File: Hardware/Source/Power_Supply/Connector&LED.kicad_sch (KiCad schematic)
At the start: 13 parts, among them J2 Conn_01x09_Socket

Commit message: update
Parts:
- J2: footprint (none) -> Connector_PinHeader_1.00mm:PinHeader_1x09_P1.00mm_Vertical
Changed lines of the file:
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@@
 			)
 		)
-		(property "Footprint" ""
+		(property "Footprint" "Connector_PinHeader_1.00mm:PinHeader_1x09_P1.00mm_Vertical"
 			(at 101.6 69.85 0)
 			(effects

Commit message: update
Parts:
- removed J2: Conn_01x09_Socket, Connector_PinHeader_1.00mm:PinHeader_1x09_P1.00mm_Vertical, symbol Connector:Conn_01x09_Socket
- added J2, J3: Conn_01x06_Socket, Connector_Phoenix_MC:PhoenixContact_MC_1,5_6-G-3.81_1x06_P3.81mm_Horizontal, symbol Connector:Conn_01x06_Socket
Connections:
- net +12V: now also J2.1 (Pin_1)
- net +5V: now also J2.4 (Pin_4), J3.1 (Pin_1)
- net +9V: now also J2.2 (Pin_2), J3.4 (Pin_4)
- net -9_1V: now also J3.5 (Pin_5)
- net -9_2V: now also J2.3 (Pin_3)
- net GND2: now also J2.6 (Pin_6), J3.6 (Pin_6)
- new net +3.3_1V: J3.2 (Pin_2)
- new net +3.3_2V: J3.3 (Pin_3)
- new net +3.3_3V: J2.5 (Pin_5)

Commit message: update flyback co 7V
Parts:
- added J4: Conn_01x02_Socket, Connector_Phoenix_MC:PhoenixContact_MC_1,5_2-G-3.5_1x02_P3.50mm_Horizontal, symbol Connector:Conn_01x02_Socket
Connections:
- net +5V: no longer J2.4 (Pin_4), J3.1 (Pin_1)
- new net +5_1V: J4.1 (Pin_1)
- new net +5_2V: J2.4 (Pin_4), J3.1 (Pin_1)
- new net GND3: J4.2 (Pin_2)
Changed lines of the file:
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@@
+	(wire
+		(pts
+			(xy 86.36 76.2) (xy 86.36 74.93)
+		)
+		(stroke
+			(width 0)
+			(type default)
+		)
+	)
 	(wire
 		(pts
@@
 	(wire
 		(pts
+			(xy 86.36 78.74) (xy 86.36 81.28)
+		)
+		(stroke
+			(width 0)
+			(type default)
+		)
+	)
+	(wire
+		(pts
 			(xy 59.69 102.87) (xy 90.17 102.87)
 		)
@@
 	(wire
 		(pts
+			(xy 90.17 76.2) (xy 86.36 76.2)
+		)
+		(stroke
+			(width 0)
+			(type default)
+		)
+	)
+	(wire
+		(pts
 			(xy 190.5 55.88) (xy 190.5 58.42)
 		)
@@
 		(pts
 			(xy 77.47 97.79) (xy 90.17 97.79)
+		)
+		(stroke
+			(width 0)
+			(type default)
+		)
+	)
+	(wire
+		(pts
+			(xy 90.17 78.74) (xy 86.36 78.74)
 		)
 		(stroke
@@
 	)
 	(symbol
+		(lib_id "Connector:Conn_01x02_Socket")
+		(at 95.25 76.2 0)
+		(unit 1)
+		(exclude_from_sim no)
+		(in_bom yes)
+		(on_board yes)
+		(dnp no)
+		(fields_autoplaced yes)
+		(property "Reference" "J4"
+			(at 96.52 76.1999 0)
+			(effects
+				(font
+					(size 1.27 1.27)
+				)
+				(justify left)
+			)
+		)
+		(property "Value" "Conn_01x02_Socket"
+			(at 96.52 78.7399 0)
+			(effects
+				(font
+					(size 1.27 1.27)
+				)
+				(justify left)
+			)
+		)
+		(property "Footprint" "Connector_Phoenix_MC:PhoenixContact_MC_1,5_2-G-3.5_1x02_P3.50mm_Horizontal"
+			(at 95.25 76.2 0)
+			(effects
+				(font
+					(size 1.27 1.27)
+				)
+				(hide yes)
+			)
+		)
+		(property "Datasheet" "~"
+			(at 95.25 76.2 0)
+			(effects
+				(font
+					(size 1.27 1.27)
+				)
+				(hide yes)
+			)
+		)
+		(property "Description" "Generic connector, single row, 01x02, script generated"
+			(at 95.25 76.2 0)
+			(effects
+				(font
+					(size 1.27 1.27)
+				)
+				(hide yes)
+			)
+		)
+		(pin "2"
+		)
+		(pin "1"
+		)
+		(instances
+			(project ""
+				(path "/5c8a7907-026b-4416-b231-5ef9f93b99e1/68308591-2b49-42fc-9085-b4eeb0133b73"
+					(reference "J4")
+					(unit 1)
+				)
+			)
+		)
+	)
+	(symbol
 		(lib_id "power:GND2")
 		(at 190.5 109.22 0)
@@
 			)
 		)
-		(property "Value" "+5V"
+		(property "Value" "+5_2V"
 			(at 63.5 129.286 0)
 			(effects
@@
 				(path "/5c8a7907-026b-4416-b231-5ef9f93b99e1/68308591-2b49-42fc-9085-b4eeb0133b73"
 					(reference "R26")
+					(unit 1)
+				)
+			)
+		)
+	)
+	(symbol
+		(lib_id "power:+3.3V")
+		(at 86.36 74.93 0)
+		(unit 1)
+		(exclude_from_sim no)
+		(in_bom yes)
+		(on_board yes)
+		(dnp no)
+		(property "Reference" "#PWR065"
+			(at 86.36 78.74 0)
+			(effects
+				(font
+					(size 1.27 1.27)
+				)
+				(hide yes)
+			)
+		)
+		(property "Value" "+5_1V"
+			(at 86.36 71.374 0)
+			(effects
+				(font
+					(size 1.27 1.27)
+				)
+			)
+		)
+		(property "Footprint" ""
+			(at 86.36 74.93 0)
+			(effects
+				(font
+					(size 1.27 1.27)
+				)
+				(hide yes)
+			)
+		)
+		(property "Datasheet" ""
+			(at 86.36 74.93 0)
+			(effects
+				(font
+					(size 1.27 1.27)
+				)
+				(hide yes)
+			)
+		)
+		(property "Description" "Power symbol creates a global label with name \"+3.3V\""
+			(at 86.36 74.93 0)
+			(effects
+				(font
+					(size 1.27 1.27)
+				)
+				(hide yes)
+			)
+		)
+		(pin "1"
+		)
+		(instances
+			(project "Power_Supply"
+				(path "/5c8a7907-026b-4416-b231-5ef9f93b99e1/68308591-2b49-42fc-9085-b4eeb0133b73"
+					(reference "#PWR065")
 					(unit 1)
 				)
@@
 	)
 	(symbol
+		(lib_id "power:GND2")
+		(at 86.36 81.28 0)
+		(unit 1)
+		(exclude_from_sim no)
+		(in_bom yes)
+		(on_board yes)
+		(dnp no)
+		(fields_autoplaced yes)
+		(property "Reference" "#PWR066"
+			(at 86.36 87.63 0)
+			(effects
+				(font
+					(size 1.27 1.27)
+				)
+				(hide yes)
+			)
+		)
+		(property "Value" "GND3"
+			(at 86.36 86.36 0)
+			(effects
+				(font
+					(size 1.27 1.27)
+				)
+			)
+		)
+		(property "Footprint" ""
+			(at 86.36 81.28 0)
+			(effects
+				(font
+					(size 1.27 1.27)
+				)
+				(hide yes)
+			)
+		)
+		(property "Datasheet" ""
+			(at 86.36 81.28 0)
+			(effects
+				(font
+					(size 1.27 1.27)
+				)
+				(hide yes)
+			)
+		)
+		(property "Description" "Power symbol creates a global label with name \"GND2\" , ground"
+			(at 86.36 81.28 0)
+			(effects
+				(font
+					(size 1.27 1.27)
+				)
+				(hide yes)
+			)
+		)
+		(pin "1"
+		)
+		(instances
+			(project "Power_Supply"
+				(path "/5c8a7907-026b-4416-b231-5ef9f93b99e1/68308591-2b49-42fc-9085-b4eeb0133b73"
+					(reference "#PWR066")
+					(unit 1)
+				)
+			)
+		)
+	)
+	(symbol
 		(lib_id "power:-9V")
 		(at 151.13 104.14 0)
@@
 			)
 		)
-		(property "Value" "+5V"
+		(property "Value" "+5_2V"
 			(at 77.47 90.424 0)
 			(effects

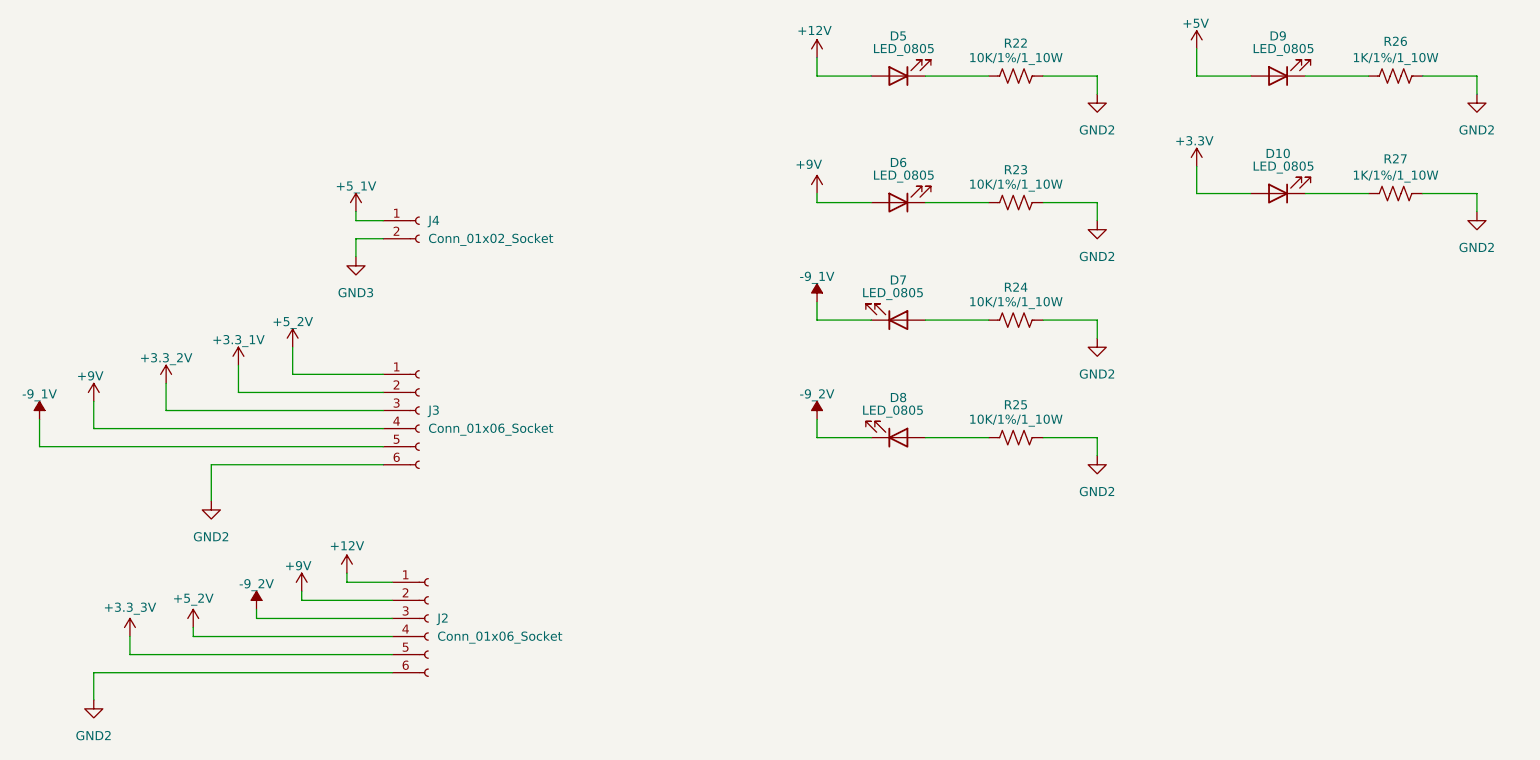
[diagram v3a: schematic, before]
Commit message: update flyback almost done
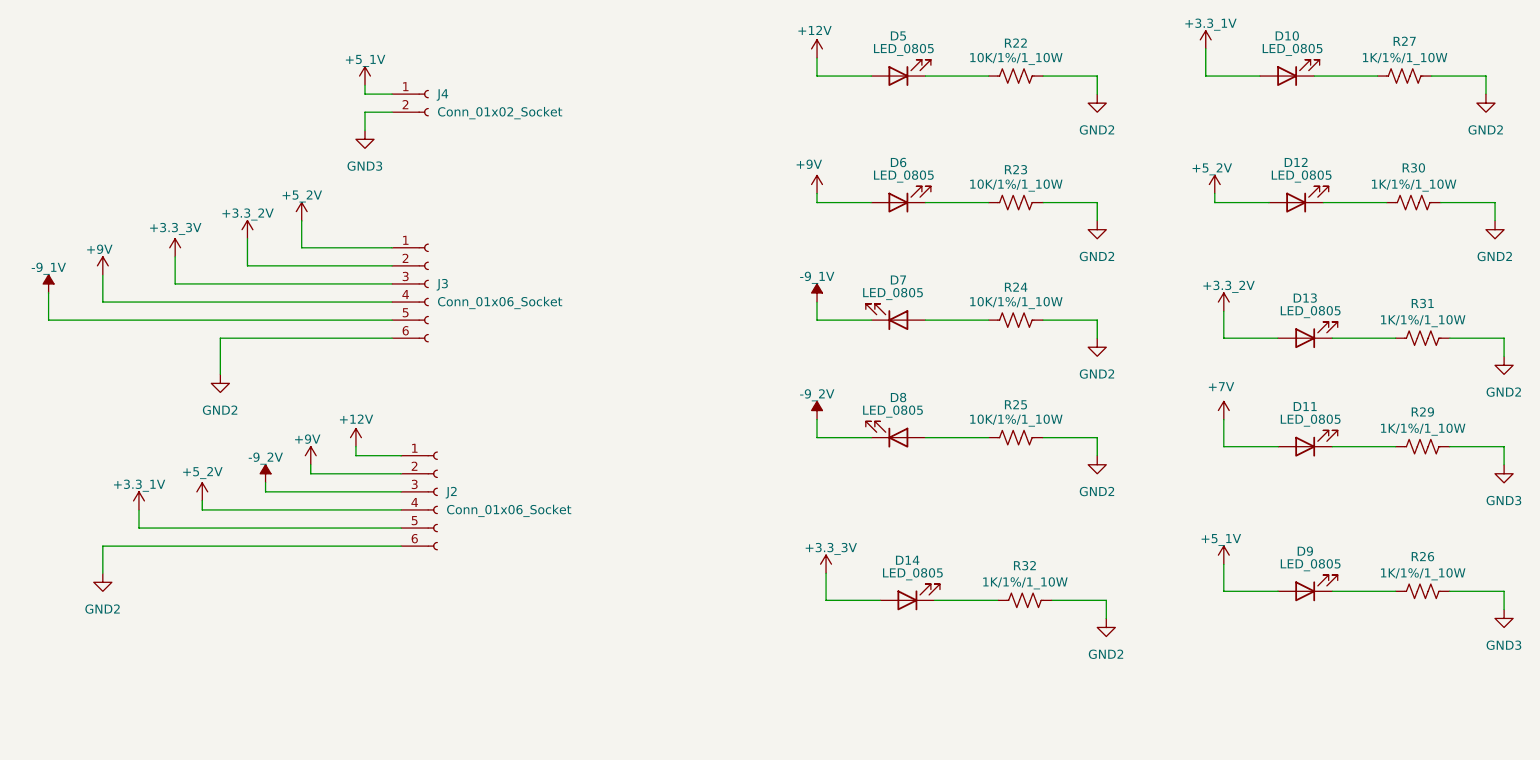
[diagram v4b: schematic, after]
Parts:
- added D11, D12, D13, D14: LED_0805, charge_battery_footprint_lib:LED_0805, symbol charge_battery_sym_lib:LED_0805
- added R29, R30, R31, R32: 1K/1%/1_10W, charge_battery_footprint_lib:Res_0603, symbol charge_battery_sym_lib:Res_1K_0603_1%
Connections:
- net +3.3V is gone; now on net +3.3_1V: D10.2 (A)
- net +5V is gone; now on net +5_1V: D9.2 (A)
- net +3.3_1V: now also J2.5 (Pin_5); no longer J3.2 (Pin_2)
- net +3.3_2V: now also J3.2 (Pin_2), D13.2 (A); no longer J3.3 (Pin_3)
- net +3.3_3V: now also J3.3 (Pin_3), D14.2 (A); no longer J2.5 (Pin_5)
- net +5_2V: now also D12.2 (A)
- net GND2: now also R30.2, R31.2, R32.2; no longer R26.2
- net GND3: now also R26.2, R29.2
- new net: D12.1 (K), R30.1
- new net: D13.1 (K), R31.1
- new net: D14.1 (K), R32.1
- new net: D11.1 (K), R29.1
- new net +7V: D11.2 (A)
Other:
- moved on the sheet: D10, D9, J2, J3, J4, R26, R27
